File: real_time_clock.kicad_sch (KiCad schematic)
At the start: 14 parts, among them U2 PCF85063A, U8 TCN75, Y1 Crystal-CM7V-T1A-32.768kHz

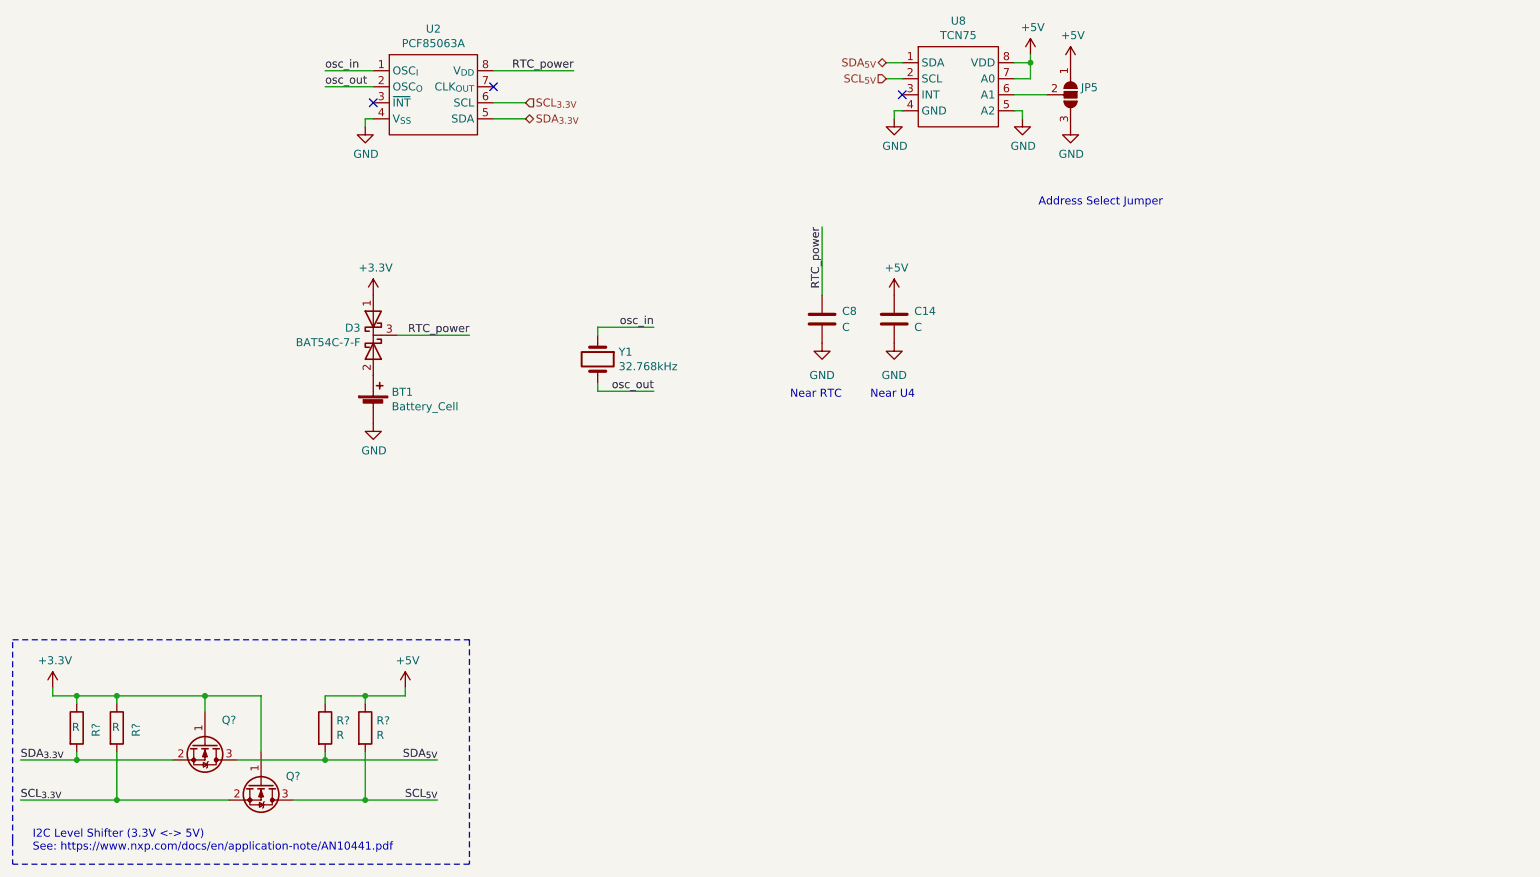
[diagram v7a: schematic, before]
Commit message: Forgot to connect the interrupt signal for the GPIO
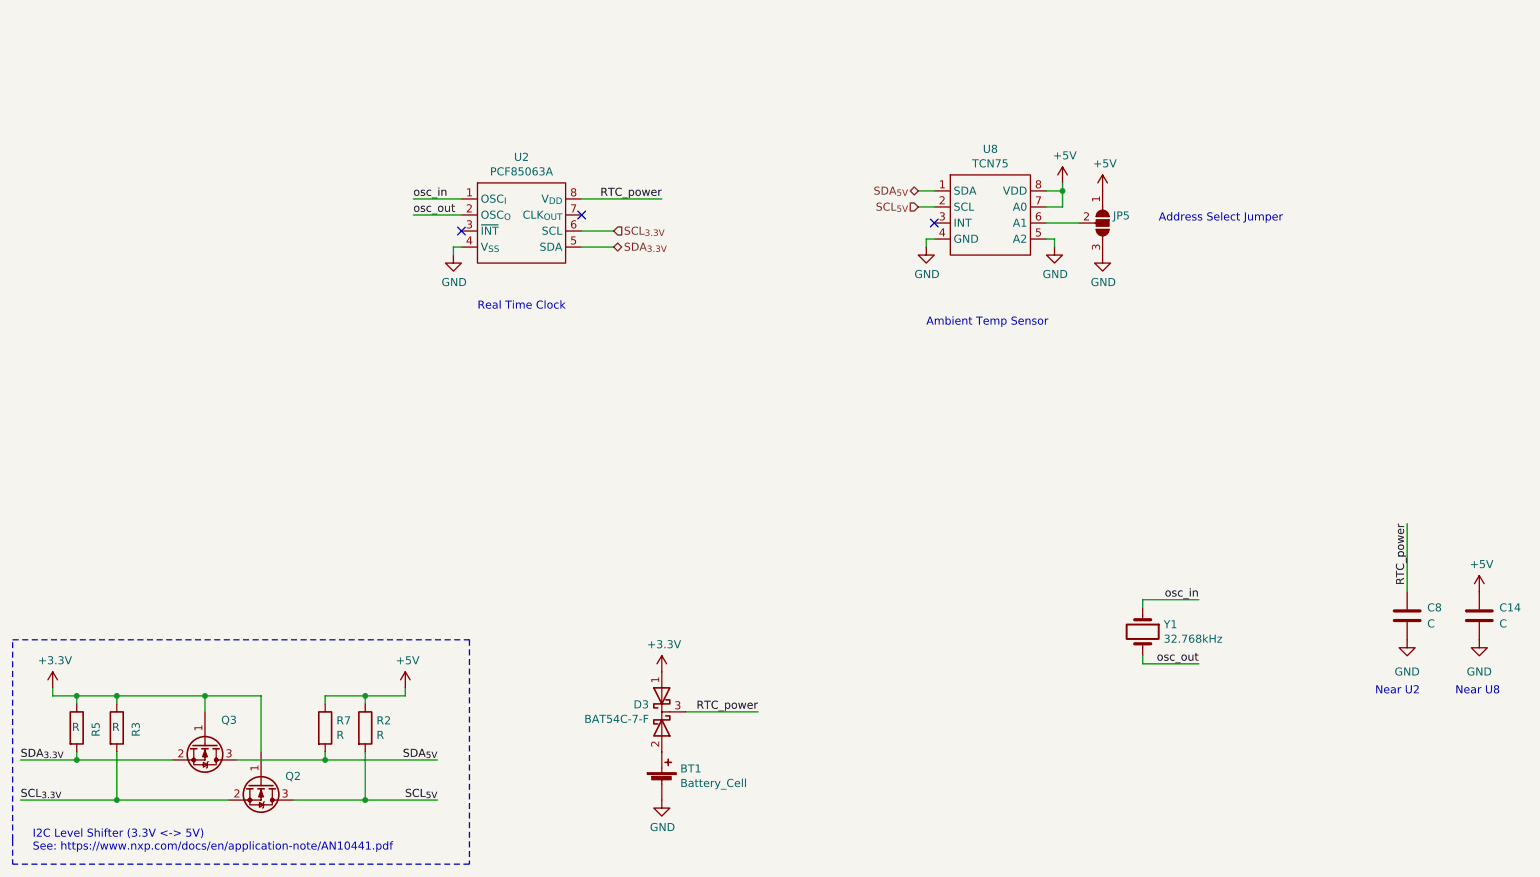
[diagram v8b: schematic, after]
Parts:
- gave numbers to parts that had none: 6
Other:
- note added: "Ambient Temp Sensor"
- note added: "Near U2"
- note added: "Near U8"
- note added: "Real Time Clock"
- note removed: "Near RTC"
- note removed: "Near U4"
- moved on the sheet: BT1, C14, C8, D3, JP5, U2, U8, Y1
